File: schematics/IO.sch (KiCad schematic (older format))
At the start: 71 parts, among them J4 Outputs, J8 Power Pins, Q1 MMBT3906, U10 TL082, U11 6S21, U12 6S21, U13 TL082, U16 TL082, U7 LM324, U8 TL082, U9 MCP4728

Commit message: PSLab V6 (#93)
* board: component placement in v6

components: added footprints for regulator and SDcard

routes: voltage regulator, SD card, SPI

components: added tact switch and routes

* board: switch to latest KiCAD version

route: fix switch routes

fix: DRC Issues fixed

docs: added new schematics PDF

docs: updated BoM for v6 PSLab

* feat: 3D models with new KiCAD version

route: VDD missing routes being fixed

route: UART routes

route: complete

3D footprints and optimization

* route: optimization

route: finalized

layout: generated gerber, svg and dxf files for production

* docs: updated BoM

* update: added spacing with more test points

* docs: verrification of BoM

* docs: updated POS files
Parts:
- added TP10, TP8, TP9: TEST, Measurement_Points:Measurement_Point_Round-SMD-Pad_Small, symbol PSLab-rescue:TEST
- C22, C23, C24, C25, C26, C27, C28, C29, C30, C31, C32, C33, C34, C35, C36, C37, C38, C39, C40, C41, C43, C6, C7: symbol C-RESCUE-proto1 -> PSLab-rescue:C-RESCUE-proto1
- J4: symbol Conn_01x12 -> PSLab-rescue:Conn_01x12
- J8: symbol Conn_01x08 -> PSLab-rescue:Conn_01x08
- Q1: symbol MMBT3906 -> PSLab-rescue:MMBT3906
- R14, R15, R16, R17, R18, R19, R20, R21, R22, R23, R24, R25, R26, R27, R28, R29, R30, R31, R32, R33, R34, R35, R36, R37, R38, R39, R40, R41, R42, R43, R44, R45, R46, R47, R50: symbol R-RESCUE-proto1 -> PSLab-rescue:R-RESCUE-proto1
- TP1, TP2: symbol TEST -> PSLab-rescue:TEST
- U10, U13, U16, U8: symbol TL082-RESCUE-proto1 -> PSLab-rescue:TL082-RESCUE-proto1
- U11, U12: symbol MCP6S21A -> PSLab-rescue:MCP6S21A
- U7: symbol LM324-RESCUE-proto1 -> PSLab-rescue:LM324-RESCUE-proto1
- U9: symbol MCP4728-RESCUE-PSLab -> PSLab:MCP4728-RESCUE-PSLab
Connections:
- net AVdd: now also TP8.1
- net V+: now also U13.8 (V+), U7.4 (V+), U7.4 (V+), U7.4 (V+)
- net V-: now also U13.4 (V-), U7.11 (V-), U7.11 (V-), U7.11 (V-)
- net VR+: now also U10.8 (V+), U16.8 (V+), U8.8 (V+), TP9.1
- net VR-: now also U10.4 (V-), U16.4 (V-), U8.4 (V-), TP10.1
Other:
- moved on the sheet: C30, C35, C36, C38, C40, C6, C7, R41, R42, R43, R50, TP1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

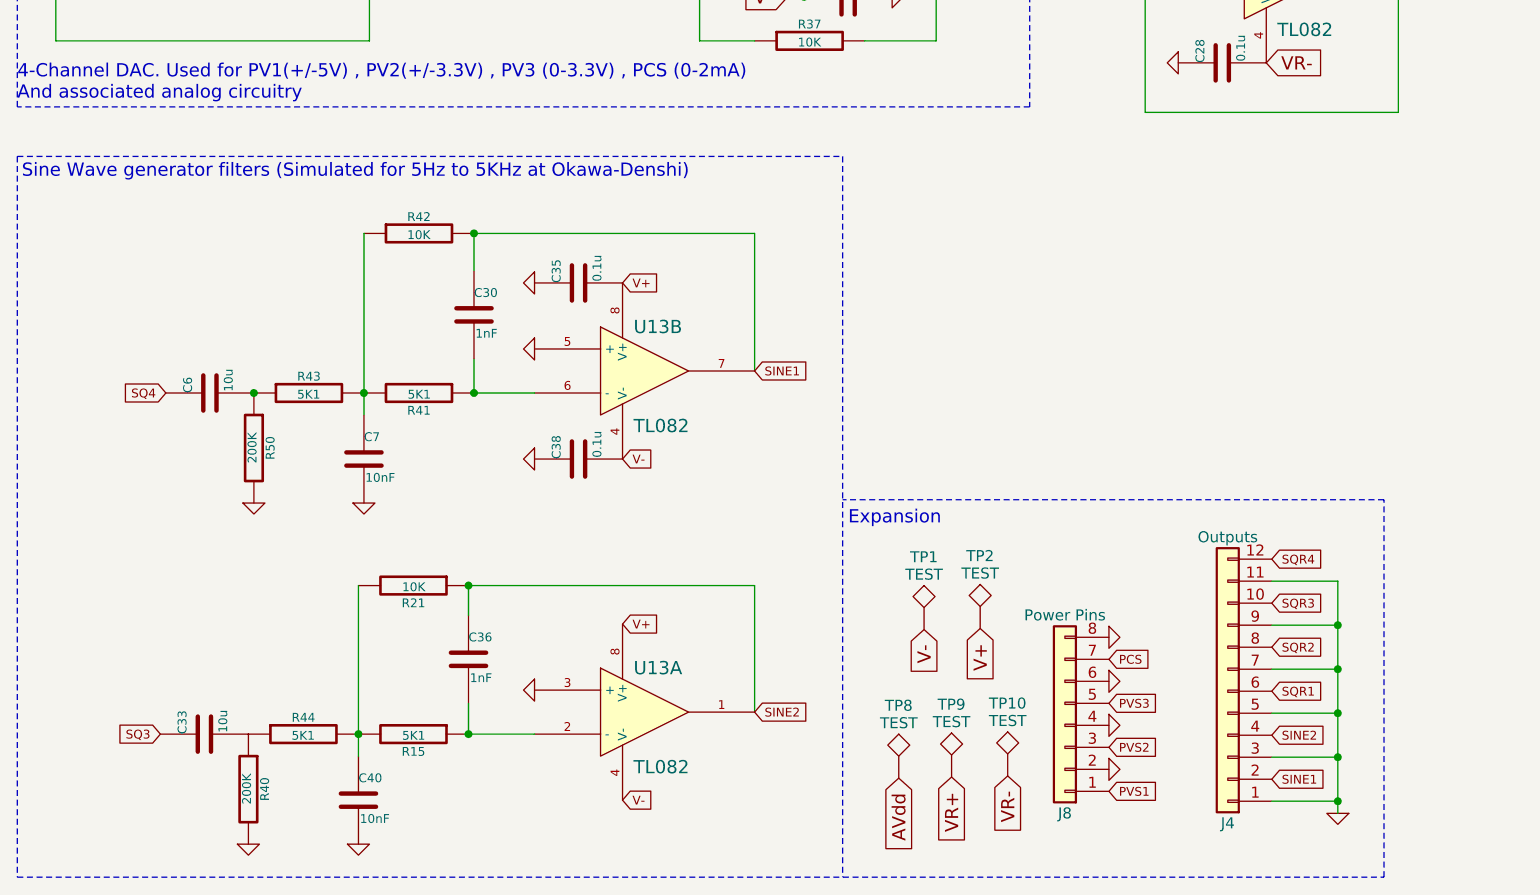
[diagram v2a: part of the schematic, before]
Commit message: feat: RTC Module
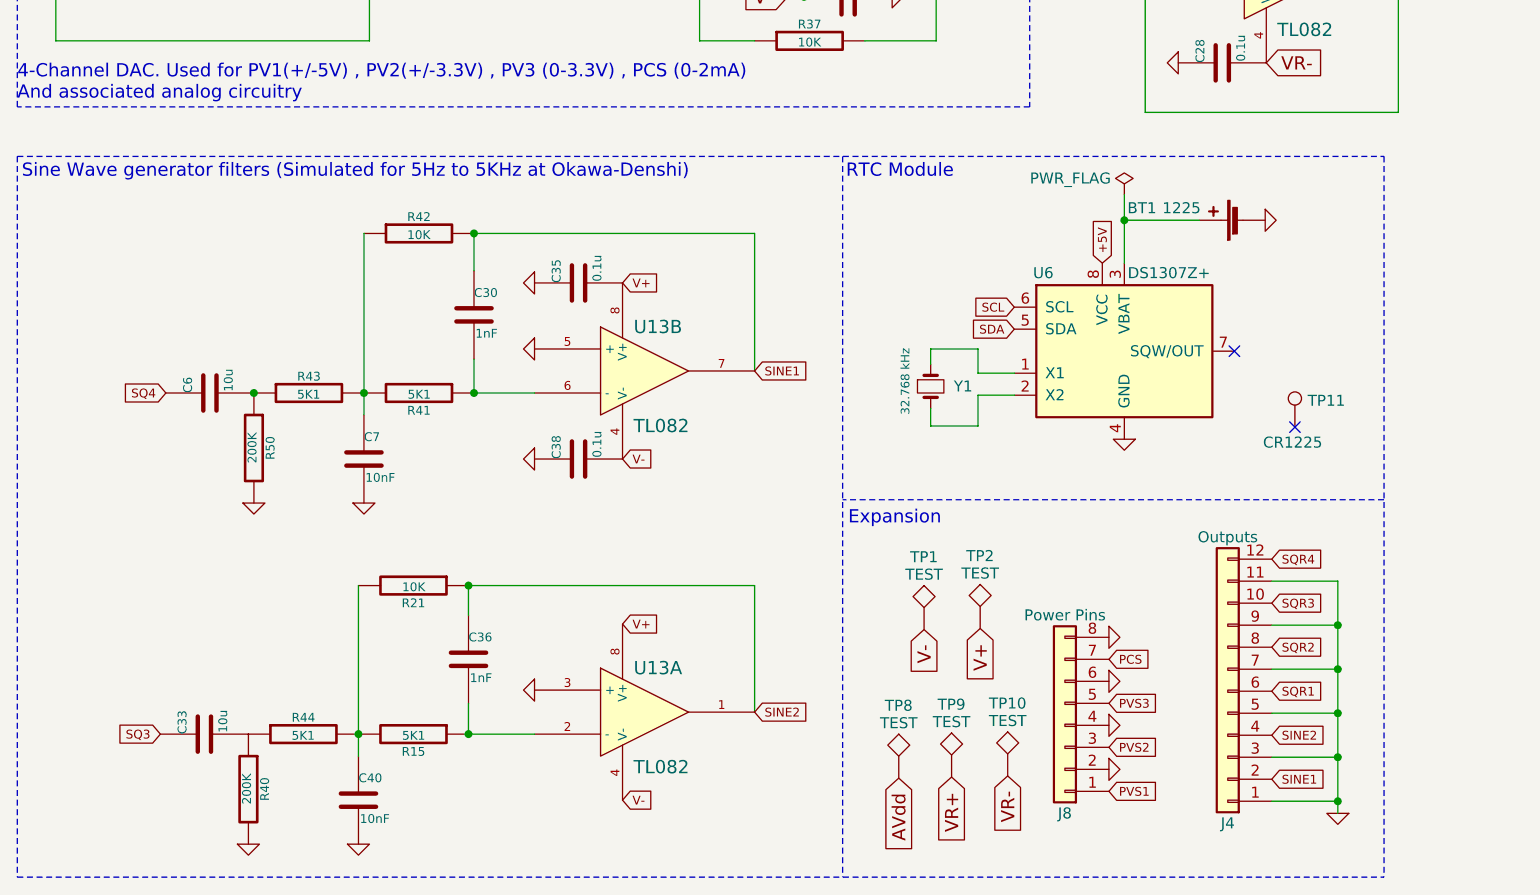
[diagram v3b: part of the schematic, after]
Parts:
- added BT1: 1225, Battery:BatteryHolder_LINX_BAT-HLD-012-SMT, symbol Device:Battery_Cell
- added TP11: CR1225, Battery:Battery_CR1225, symbol Connector:TestPoint
- added U6: DS1307Z+, Package_SO:SOIC-8_3.9x4.9mm_P1.27mm, symbol Timer_RTC:DS1307Z+
- added Y1: 32.768 kHz, Crystal:Crystal_SMD_3215-2Pin_3.2x1.5mm, symbol Device:Crystal_Small
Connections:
- net GND: now also BT1.2 (-), U6.4 (GND)
- net SCL: now also U6.6 (SCL)
- net SDA: now also U6.5 (SDA)
- new net: U6.1 (X1), Y1.1
- new net: U6.2 (X2), Y1.2
- new net: BT1.1 (+), U6.3 (VBAT)
- new net +5V: U6.8 (VCC)
- no-connect marks 1 -> 3
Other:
- note added: "RTC Module"
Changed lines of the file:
@@
 4-Channel DAC. Used for PV1(+/-5V) , PV2(+/-3.3V) , PV3 (0-3.3V) , PCS (0-2mA)\nAnd associated analog circuitry
-Wire Notes Line
-	550  4175 4300 4175
 Wire Notes Line
 	550  4175 550  7450
@@
 Text Notes 4325 5855 0    60   ~ 0
 Expansion
-Wire Notes Line
-	6760 7450 6760 5735
 $Comp
 L PSLab-rescue:Conn_01x12 J4
@@
 Text GLabel 4555 7000 3    60   Input ~ 0
 AVdd
+Wire Notes Line
+	550  4175 6760 4175
+Wire Notes Line
+	6760 4175 6760 7450
+Text Notes 4315 4280 0    60   ~ 0
+RTC Module
+$Comp
+L Timer_RTC:DS1307Z+ U6
+U 1 1 5CA94FBE
+P 5580 5060
+F 0 "U6" H 5165 5415 50  0000 L CNN
+F 1 "DS1307Z+" H 5595 5415 50  0000 L CNN
+F 2 "Package_SO:SOIC-8_3.9x4.9mm_P1.27mm" H 5580 4560 50  0001 C CNN
+F 3 "https://datasheets.maximintegrated.com/en/ds/DS1307.pdf" H 5580 5060 50  0001 C CNN
+	1    5580 5060
+	1    0    0    -1
+$EndComp
+$Comp
+L Device:Crystal_Small Y1
+U 1 1 5CA951B5
+P 4700 5220
+F 0 "Y1" V 4700 5325 50  0000 L CNN
+F 1 "32.768 kHz" H 4525 5105 39  0000 L CNN
+F 2 "Crystal:Crystal_SMD_3215-2Pin_3.2x1.5mm" H 4700 5220 50  0001 C CNN
+F 3 "~" H 4700 5220 50  0001 C CNN
+	1    4700 5220
+	0    1    1    0
+$EndComp
+Wire Wire Line
+	4700 5120 4700 5050
+Wire Wire Line
+	4700 5050 4915 5050
+Wire Wire Line
+	4915 5050 4915 5160
+Wire Wire Line
+	4915 5160 5080 5160
+Wire Wire Line
+	4700 5320 4700 5400
+Wire Wire Line
+	4700 5400 4915 5400
+Wire Wire Line
+	4915 5400 4915 5260
+Wire Wire Line
+	4915 5260 5080 5260
+$Comp
+L PSLab-rescue:GND-RESCUE-proto1 #PWR?
+U 1 1 5CAA467A
+P 5580 5460
+AR Path="/5CAA467A" Ref="#PWR?"  Part="1"
+AR Path="/54260FB5/5CAA467A" Ref="#PWR010"  Part="1"
+F 0 "#PWR010" H 5580 5460 30  0001 C CNN
+F 1 "GND" H 5580 5390 30  0001 C CNN
+F 2 "" H 5580 5460 60  0000 C CNN
+F 3 "" H 5580 5460 60  0000 C CNN
+	1    5580 5460
+	-1   0    0    -1
+$EndComp
+$Comp
+L Device:Battery_Cell BT1
+U 1 1 5CAA5A87
+P 6120 4465
+F 0 "BT1" V 6175 4925 50  0000 C CNN
+F 1 "1225" V 6175 4745 50  0000 C CNN
+F 2 "Battery:BatteryHolder_LINX_BAT-HLD-012-SMT" V 6120 4525 50  0001 C CNN
+F 3 "~" V 6120 4525 50  0001 C CNN
+	1    6120 4465
+	0    -1   -1   0
+$EndComp
+Wire Wire Line
+	5920 4465 5580 4465
+Wire Wire Line
+	5580 4465 5580 4660
+$Comp
+L PSLab-rescue:GND-RESCUE-proto1 #PWR?
+U 1 1 5CAAD598
+P 6220 4465
+AR Path="/5CAAD598" Ref="#PWR?"  Part="1"
+AR Path="/54260FB5/5CAAD598" Ref="#PWR021"  Part="1"
+F 0 "#PWR021" H 6220 4465 30  0001 C CNN
+F 1 "GND" H 6220 4395 30  0001 C CNN
+F 2 "" H 6220 4465 60  0000 C CNN
+F 3 "" H 6220 4465 60  0000 C CNN
+	1    6220 4465
+	0    -1   1    0
+$EndComp
+NoConn ~ 6080 5060
+Text GLabel 5080 4860 0    40   Input ~ 0
+SCL
+Text GLabel 5080 4960 0    40   Input ~ 0
+SDA
+Text GLabel 5480 4660 1    40   Input ~ 0
++5V
+Wire Wire Line
+	5580 4350 5580 4465
+Connection ~ 5580 4465
+$Comp
+L power:PWR_FLAG #FLG0101
+U 1 1 5CAE0079
+P 5580 4350
+F 0 "#FLG0101" H 5580 4425 50  0001 C CNN
+F 1 "PWR_FLAG" H 5335 4425 50  0000 C CNN
+F 2 "" H 5580 4350 50  0001 C CNN
+F 3 "~" H 5580 4350 50  0001 C CNN
+	1    5580 4350
+	1    0    0    -1
+$EndComp
+$Comp
+L Connector:TestPoint TP11
+U 1 1 5CAF8DB5
+P 6355 5405
+F 0 "TP11" H 6413 5525 50  0000 L CNN
+F 1 "CR1225" H 6210 5335 50  0000 L CNN
+F 2 "Battery:Battery_CR1225" H 6555 5405 50  0001 C CNN
+F 3 "~" H 6555 5405 50  0001 C CNN
+	1    6355 5405
+	1    0    0    -1
+$EndComp
+NoConn ~ 6355 5405
 $EndSCHEMATC
